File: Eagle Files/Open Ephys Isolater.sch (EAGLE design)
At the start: 26 parts, among them J1 DC_POWER_JACK-PJ-102AH

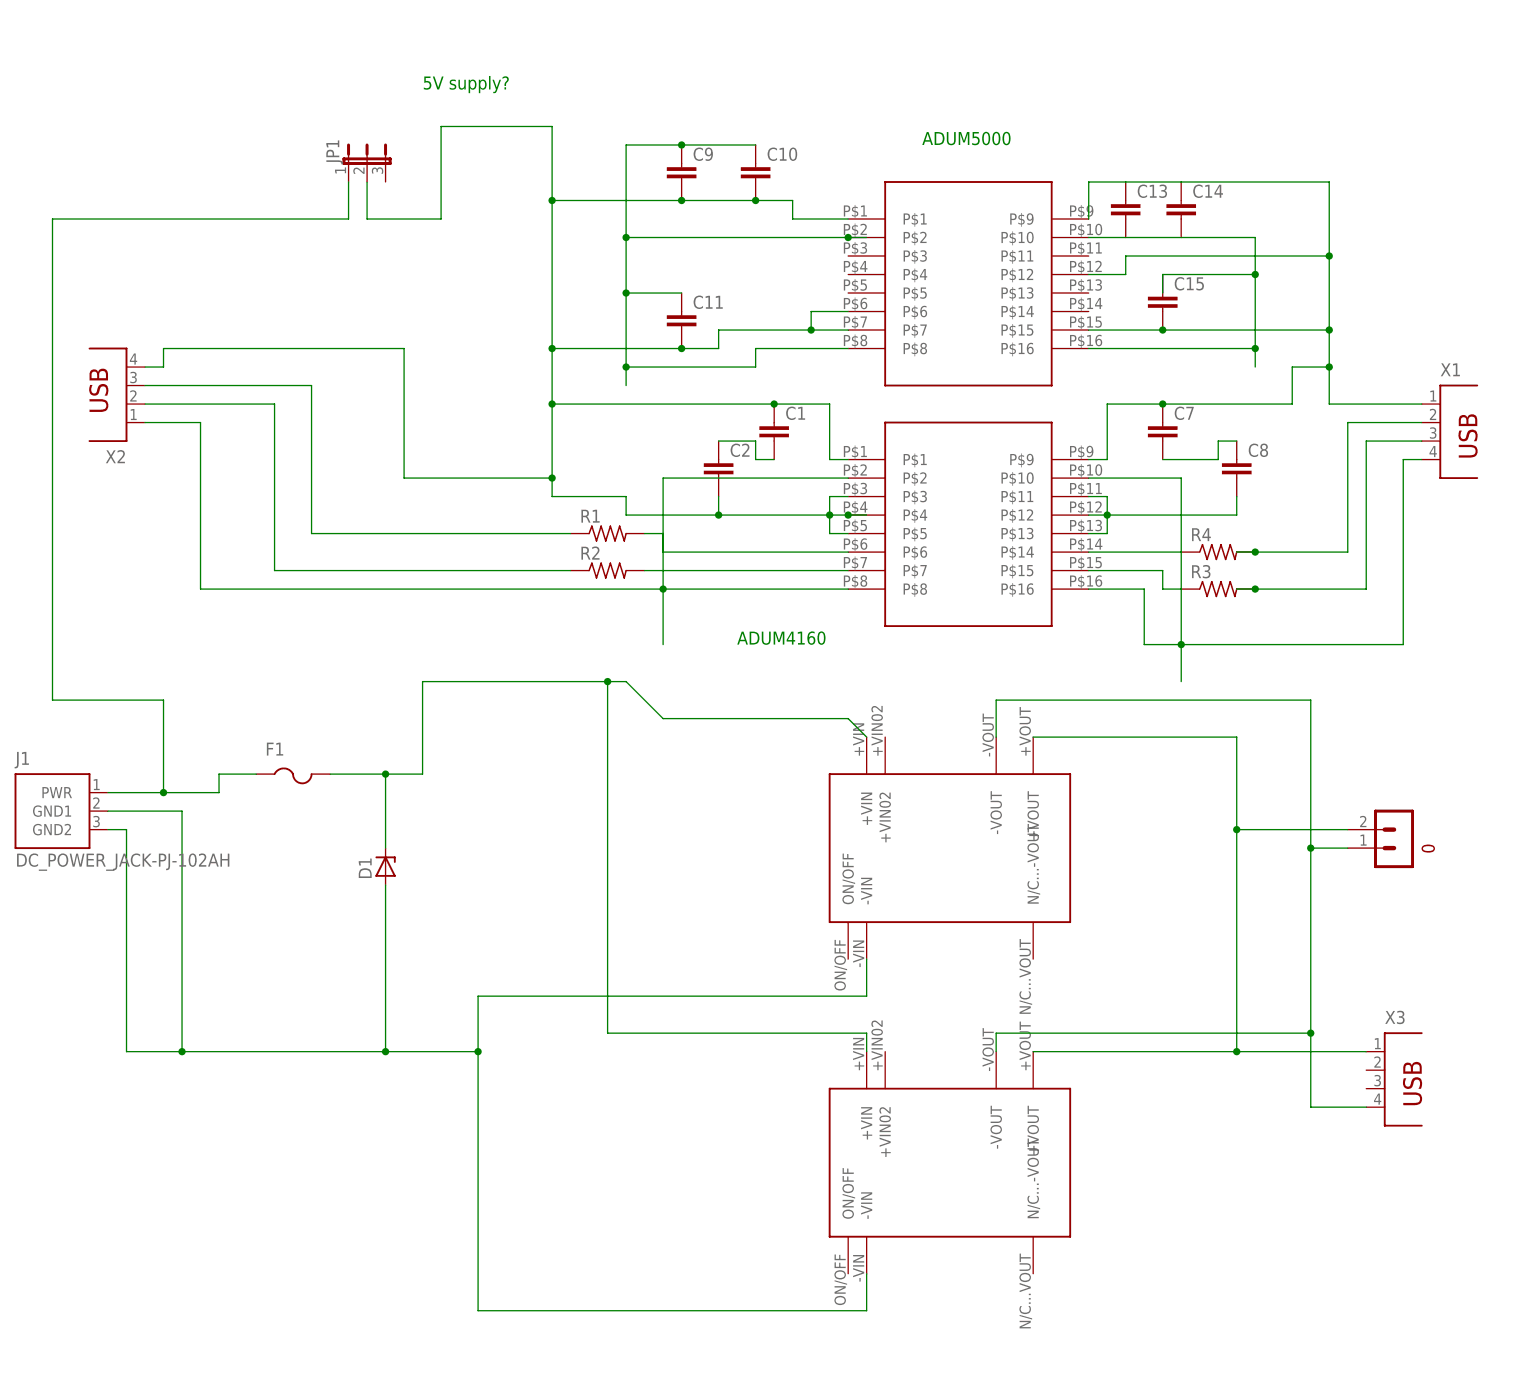
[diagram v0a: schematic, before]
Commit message: neatened nets on schematic
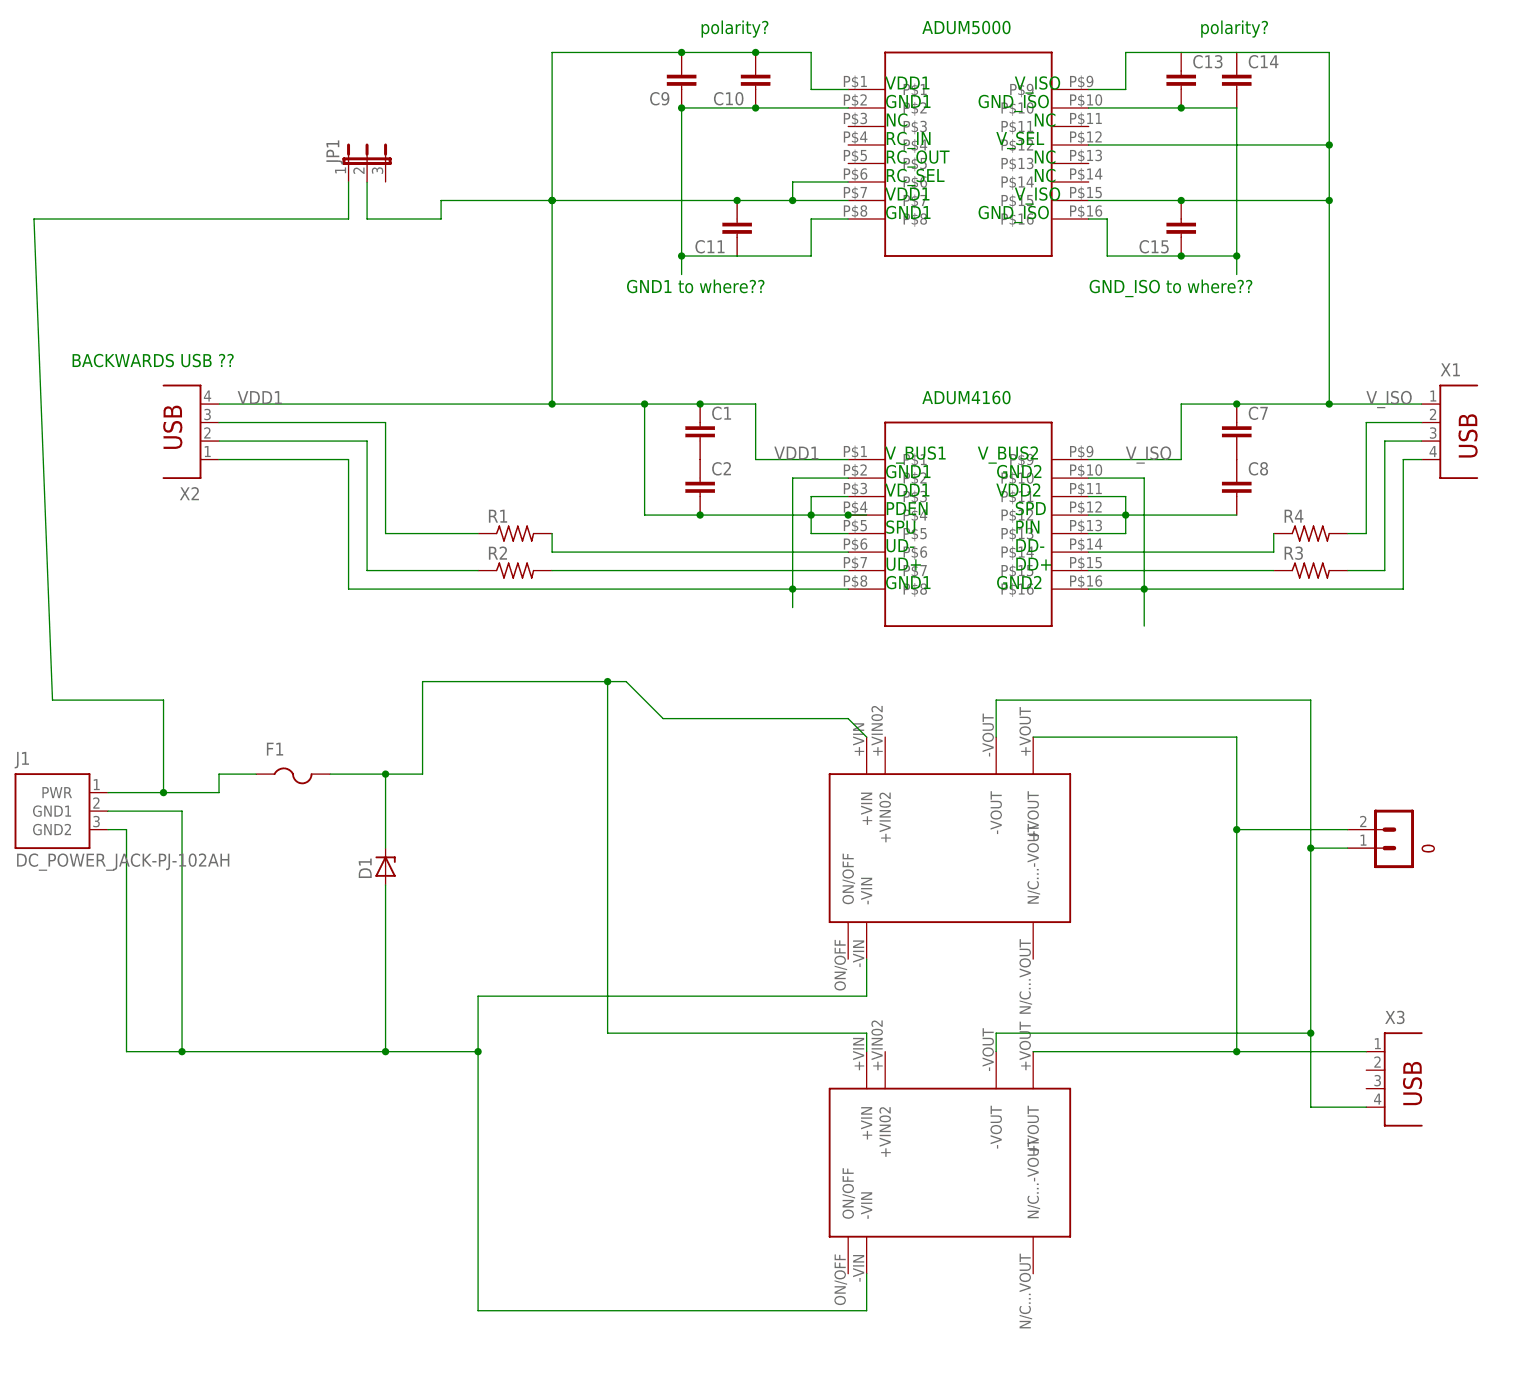
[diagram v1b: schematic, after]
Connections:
- net N$18 renamed V_ISO
- net N$4 renamed VDD1
- removed net N$16: C10.1, C11.1, C9.1, U$1.P$2, U$1.P$8
- net GND1: now also C10.1, C11.1, C9.1, U$1.P$2, U$1.P$8
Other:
- note added: "BACKWARDS USB ??"
- note added: "DD+"
- note added: "DD-"
- note added: "GND1"
- note added: "GND1 to where??"
- note added: "GND2"
- note added: "GND_ISO"
- note added: "GND_ISO to where??"
- note added: "NC"
- note added: "PDEN"
- note added: "PIN"
- note added: "RC_IN"
- note added: "RC_OUT"
- note added: "RC_SEL"
- note added: "SPD"
- note added: "SPU"
- note added: "UD+"
- note added: "UD-"
- note added: "VDD1"
- note added: "VDD2"
- note added: "V_BUS1"
- note added: "V_BUS2"
- note added: "V_ISO"
- note added: "V_SEL"
- note added: "polarity?"
- note removed: "5V supply?"
- moved on the sheet: C1, C10, C11, C13, C14, C15, C2, C7, C8, C9, R1, R2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

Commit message: more names, labels, neatening
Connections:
- removed net N$2: C13.2, C14.2, C15.1, U$1.P$10, U$1.P$16
- net GND2: now also C13.2, C14.2, C15.1, U$1.P$10, U$1.P$16
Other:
- note added: "TO GND1"
- note added: "TO GND2"
- note added: "WHATS THAT?"
- note removed: "GND1 to where??"
- note removed: "GND_ISO to where??"
- moved on the sheet: D1, F1, J1, X1, X2

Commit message: cleaned up schematic
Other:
- note added: "NCM6?"
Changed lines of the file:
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@@
 <text x="71.12" y="27.94" size="1.778" layer="91">TO GND2</text>
 <text x="109.22" y="5.08" size="1.778" layer="91">WHATS THAT?</text>
+<text x="45.72" y="-7.62" size="1.778" layer="91">NCM6?</text>
+<text x="45.72" y="-50.8" size="1.778" layer="91">NCM6?</text>
 </plain>
 <instances>
